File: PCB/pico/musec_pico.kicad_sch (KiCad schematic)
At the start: 63 parts, among them J1 Pedal, J2 PJ313, J3 PJ313, SW1 SW_DIP_x01, SW2 SW_DIP_x01, SW3 SW_DIP_x01, SW4 SW_DIP_x01, SW5 SW_DIP_x01, SW6 SW_DIP_x01, SW7 SW_DIP_x01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

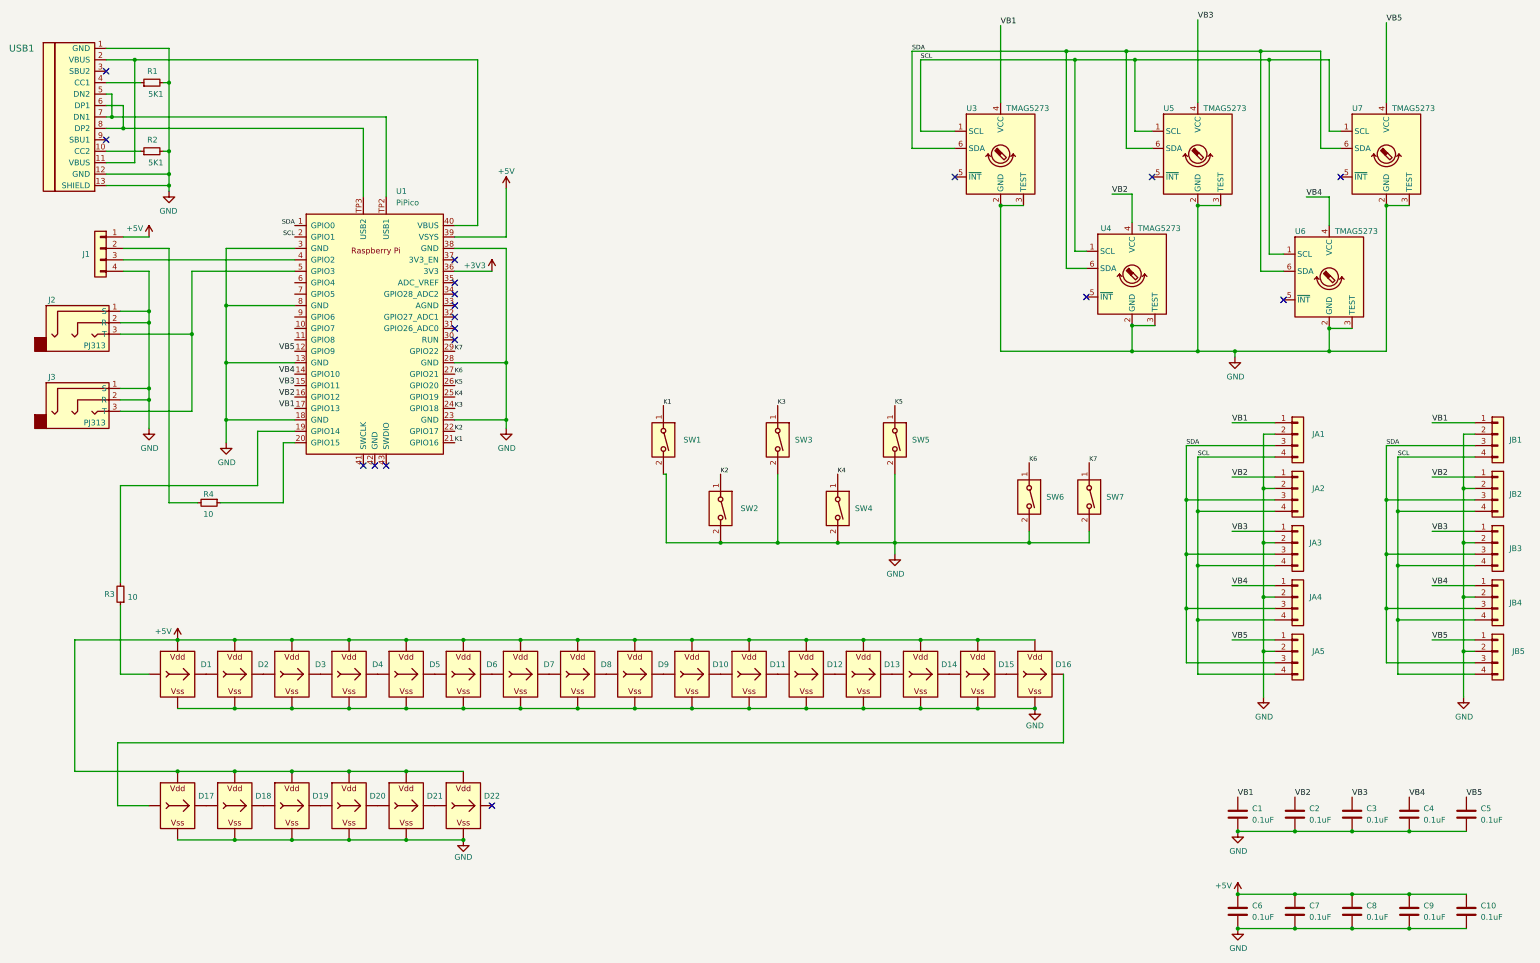
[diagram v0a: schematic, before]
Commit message: Explicit I2C Pull-ups
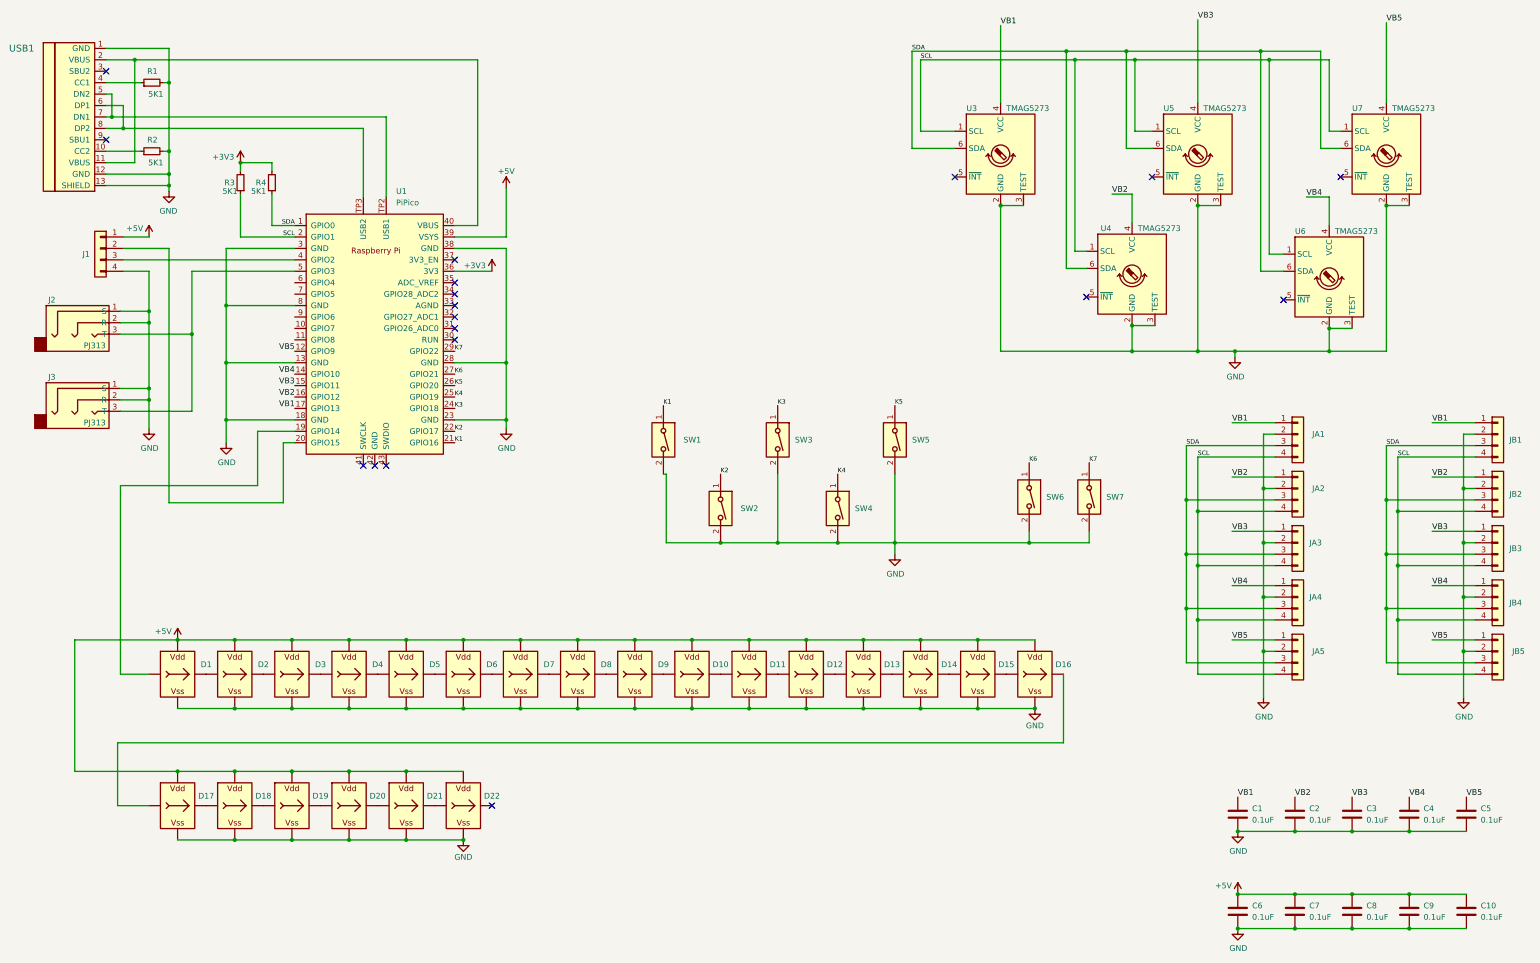
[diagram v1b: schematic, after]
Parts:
- R3, R4: value 10 -> 5K1
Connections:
- net +3V3: now also R3.2, R4.2
- net SCL: now also R3.1
- net SDA: now also R4.1
- net at D1.I (In): now also U1.19 (GPIO14); no longer R3.1
- net at J1.2 (Pin_2): now also U1.20 (GPIO15); no longer R4.2
